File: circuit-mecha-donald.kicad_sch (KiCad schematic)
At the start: 38 parts, among them J1 ST-LINK, J10 MD6, J11 ENC1, J12 ENC2, J13 ENC3, J14 ENC4, J15 ENC5, J16 ENC6, J2 CAN, J3 UART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

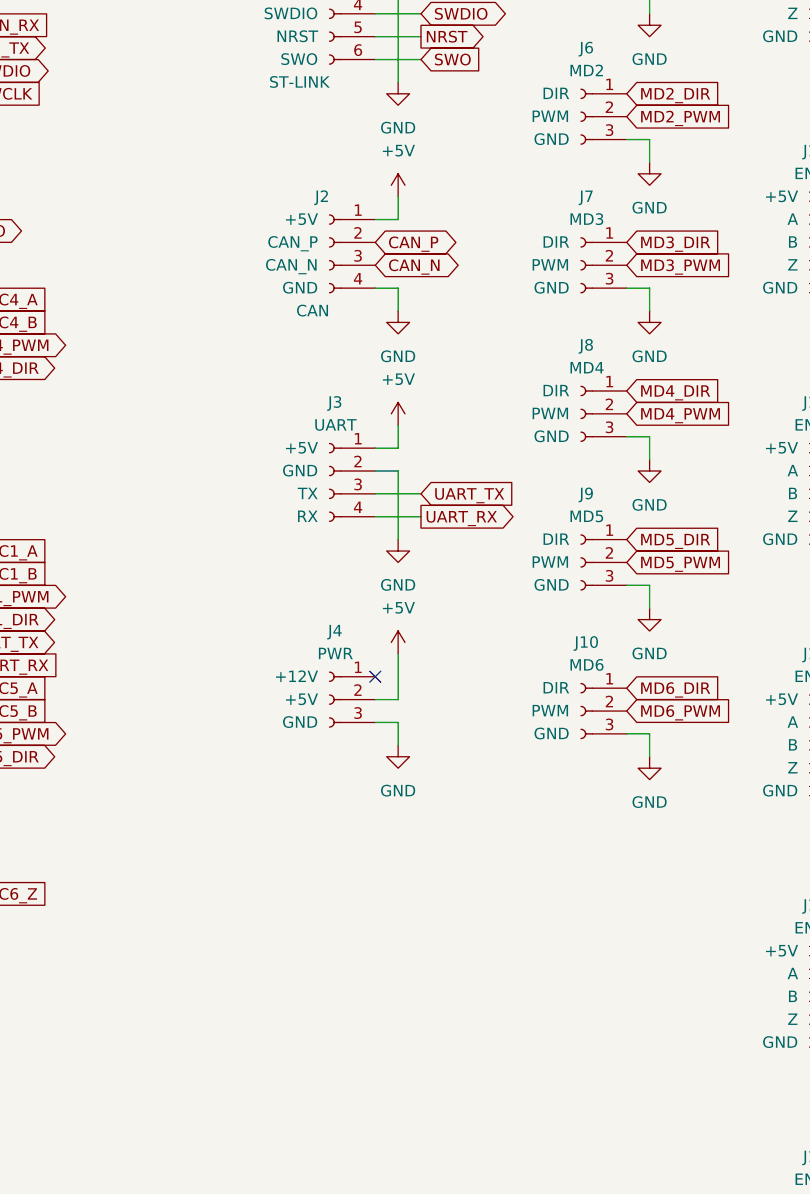
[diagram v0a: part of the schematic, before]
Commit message: feature: CANコネクタを追加。
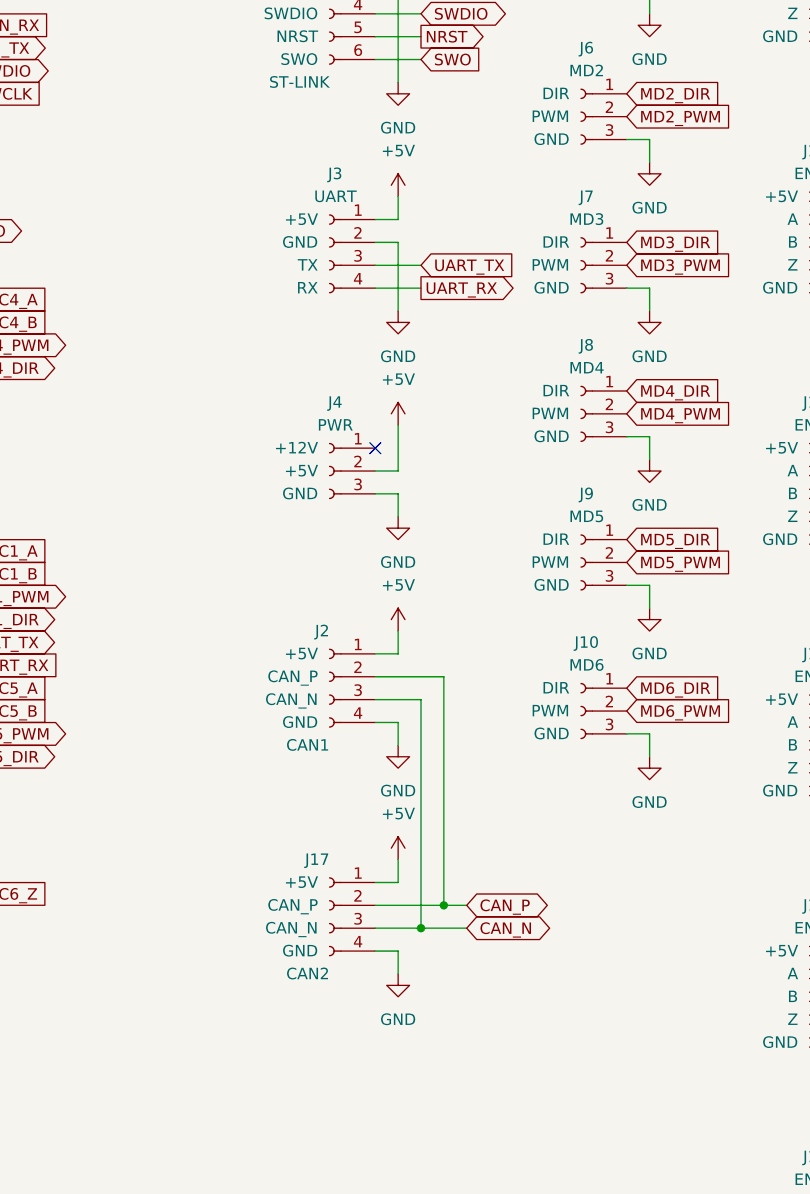
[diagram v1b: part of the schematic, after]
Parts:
- added J17: CAN2, Connector_JST:JST_XA_B04B-XASK-1_1x04_P2.50mm_Vertical, symbol circuit-mecha-donald:CAN
- J2: value CAN -> CAN1
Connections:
- net +5V: now also J17.1 (+5V)
- net CAN_N: now also J17.3 (CAN_N)
- net CAN_P: now also J17.2 (CAN_P)
- net GND: now also J17.4 (GND)
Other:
- moved on the sheet: J2, J3, J4
